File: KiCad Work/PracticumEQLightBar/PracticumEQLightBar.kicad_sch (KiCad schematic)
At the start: 54 parts, among them J1 AudioJack3Pin, U1 TEENSY 4.1, U2 TEENSY AUDIO ADAPTER BOARD RE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

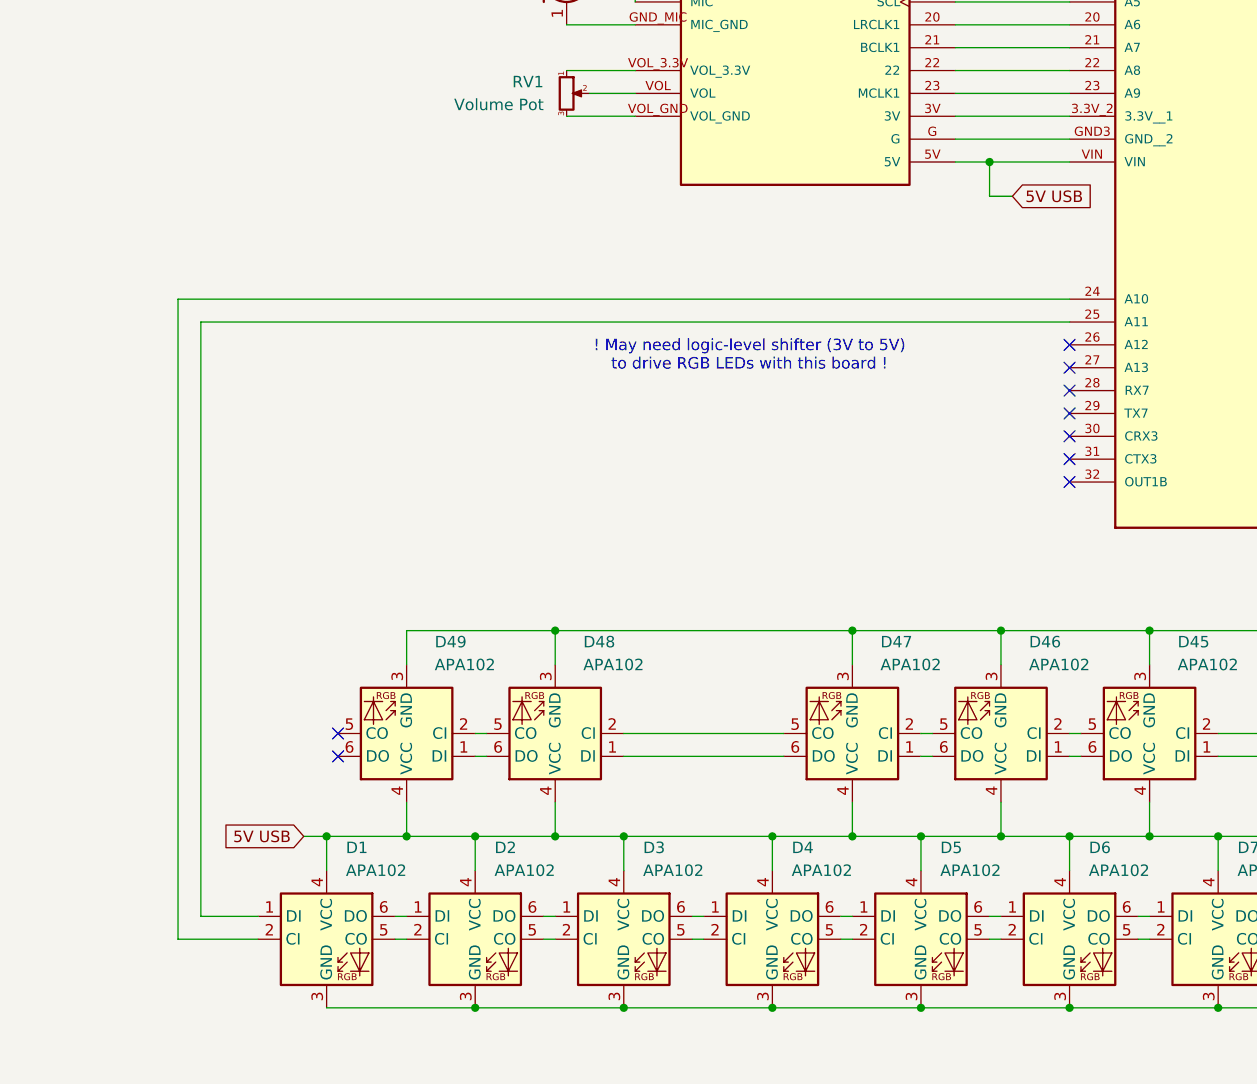
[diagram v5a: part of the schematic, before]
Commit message: Added SN74 logic level shifter to schematic and PCB
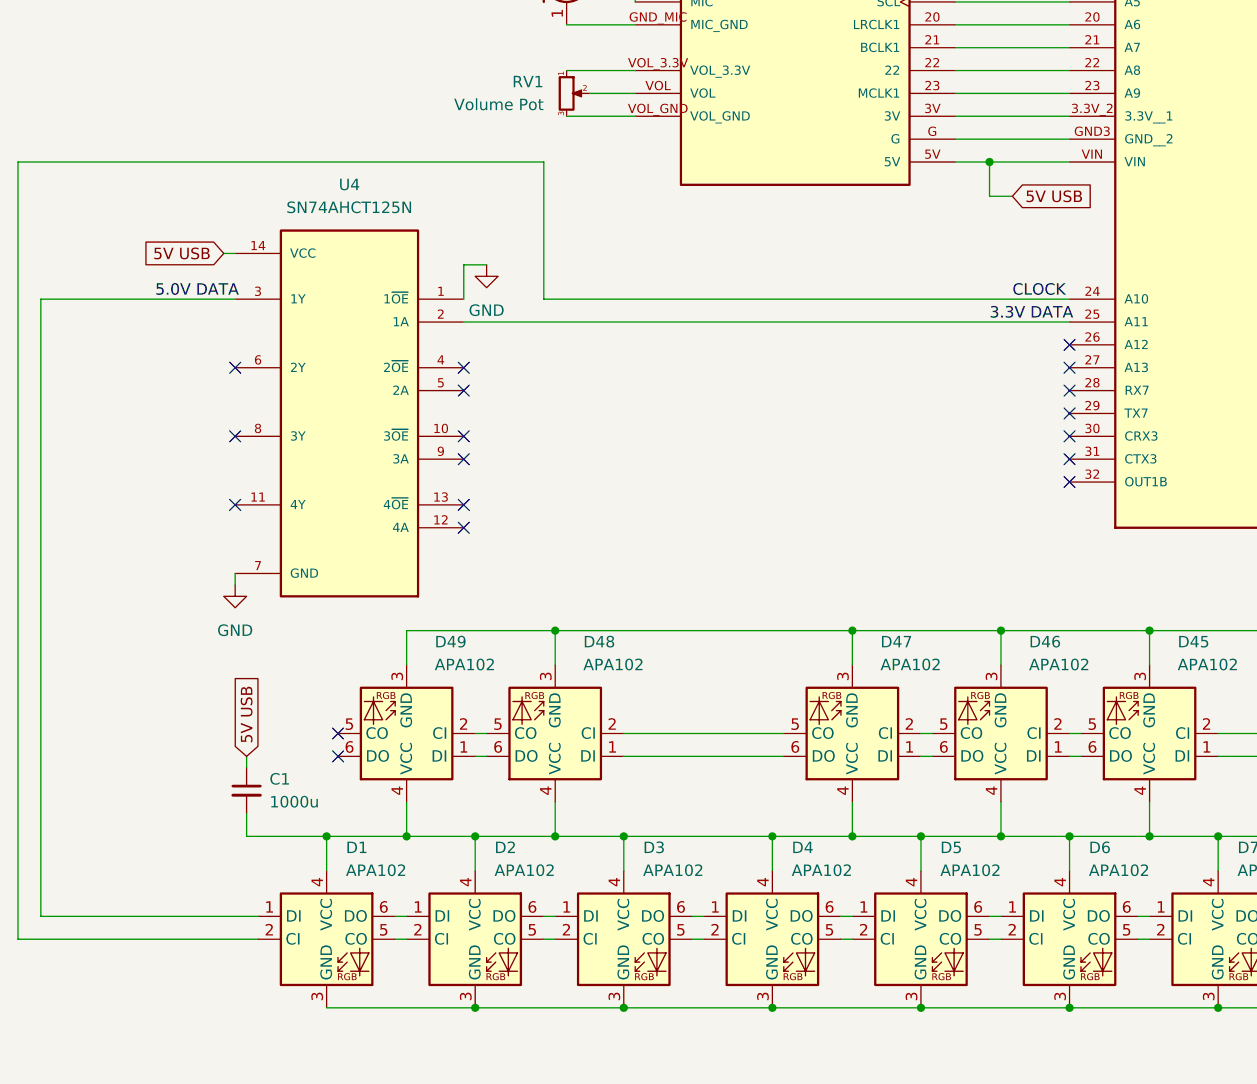
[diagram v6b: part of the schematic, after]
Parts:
- added C1: 1000u, symbol Device:C_Small
- added U4: SN74AHCT125N, SN74AHCT125N:DIP794W45P254L1930H508Q14, symbol SN74AHCT125N:SN74AHCT125N
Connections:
- net 5V USB: now also C1.1, U4.14 (VCC); no longer D1.4 (VCC), D10.4 (VCC), D11.4 (VCC), D12.4 (VCC), D13.4 (VCC), D14.4 (VCC), D15.4 (VCC), D16.4 (VCC), D17.4 (VCC), D18.4 (VCC), D19.4 (VCC), D2.4 (VCC), D20.4 (VCC), D21.4 (VCC), D22.4 (VCC), D23.4 (VCC), D24.4 (VCC), D25.4 (VCC), D26.4 (VCC), D27.4 (VCC), D28.4 (VCC), D29.4 (VCC), D3.4 (VCC), D30.4 (VCC), D31.4 (VCC), D32.4 (VCC), D33.4 (VCC), D34.4 (VCC), D35.4 (VCC), D36.4 (VCC), D37.4 (VCC), D38.4 (VCC), D39.4 (VCC), D4.4 (VCC), D40.4 (VCC), D41.4 (VCC), D42.4 (VCC), D43.4 (VCC), D44.4 (VCC), D45.4 (VCC), D46.4 (VCC), D47.4 (VCC), D48.4 (VCC), D49.4 (VCC), D5.4 (VCC), D6.4 (VCC), D7.4 (VCC), D8.4 (VCC), D9.4 (VCC)
- net GND: now also U4.1 (1~{OE}), U4.7 (GND)
- net CLOCK: now reaches D1.2 (CI), U1.24 (A10)
- net 3.3V DATA: now reaches U1.25 (A11)
- net 3.3V DATA: now also U4.2 (1A); no longer D1.1 (DI)
- new net: C1.2, D1.4 (VCC), D10.4 (VCC), D11.4 (VCC), D12.4 (VCC), D13.4 (VCC), D14.4 (VCC), D15.4 (VCC), D16.4 (VCC), D17.4 (VCC), D18.4 (VCC), D19.4 (VCC), D2.4 (VCC), D20.4 (VCC), D21.4 (VCC), D22.4 (VCC), D23.4 (VCC), D24.4 (VCC), D25.4 (VCC), D26.4 (VCC), D27.4 (VCC), D28.4 (VCC), D29.4 (VCC), D3.4 (VCC), D30.4 (VCC), D31.4 (VCC), D32.4 (VCC), D33.4 (VCC), D34.4 (VCC), D35.4 (VCC), D36.4 (VCC), D37.4 (VCC), D38.4 (VCC), D39.4 (VCC), D4.4 (VCC), D40.4 (VCC), D41.4 (VCC), D42.4 (VCC), D43.4 (VCC), D44.4 (VCC), D45.4 (VCC), D46.4 (VCC), D47.4 (VCC), D48.4 (VCC), D49.4 (VCC), D5.4 (VCC), D6.4 (VCC), D7.4 (VCC), D8.4 (VCC), D9.4 (VCC)
- new net 5.0V DATA: D1.1 (DI), U4.3 (1Y)
- no-connect marks 40 -> 49
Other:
- note removed: "! May need logic-level shifter (3V to 5V) to drive RGB LEDs with this board !"

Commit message: Updated rev 1.1 drawing sheet PDFs
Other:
- moved on the sheet: C1, D1, D10, D11, D12, D13, D14, D15, D16, D17, D18, D19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

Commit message: Commited wrong version last time
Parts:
- removed C1: 1000u, symbol Device:C_Small
- added TP1, TP2: TestPoint_Alt, TestPoint:TestPoint_Pad_1.5x1.5mm, symbol Connector:TestPoint_Alt
- U1: footprint EQLightBarLibrary:MODULE_DEV-16771 -> EQLightBarLibrary:Double PinSocket_1x24_P2.54mm_Vertical (Teensy 4_1)
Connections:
- net 3.3V DATA: now also U4.5 (2A), TP2.1; no longer U4.2 (1A)
- net 5V USB: now also D1.4 (VCC), D10.4 (VCC), D11.4 (VCC), D12.4 (VCC), D13.4 (VCC), D14.4 (VCC), D15.4 (VCC), D16.4 (VCC), D17.4 (VCC), D18.4 (VCC), D19.4 (VCC), D2.4 (VCC), D20.4 (VCC), D21.4 (VCC), D22.4 (VCC), D23.4 (VCC), D24.4 (VCC), D25.4 (VCC), D26.4 (VCC), D27.4 (VCC), D28.4 (VCC), D29.4 (VCC), D3.4 (VCC), D30.4 (VCC), D31.4 (VCC), D32.4 (VCC), D33.4 (VCC), D34.4 (VCC), D35.4 (VCC), D36.4 (VCC), D37.4 (VCC), D38.4 (VCC), D39.4 (VCC), D4.4 (VCC), D40.4 (VCC), D41.4 (VCC), D42.4 (VCC), D43.4 (VCC), D44.4 (VCC), D45.4 (VCC), D46.4 (VCC), D47.4 (VCC), D48.4 (VCC), D49.4 (VCC), D5.4 (VCC), D6.4 (VCC), D7.4 (VCC), D8.4 (VCC), D9.4 (VCC)
- net CLOCK: now also U4.2 (1A), TP1.1; no longer D1.2 (CI)
- net GND: now also U4.4 (2~{OE})
- net at U4.6 (2Y): now also D1.1 (DI)
- net 5.0V DATA: no longer names the net of U4.3 (1Y)
- net 5.0V DATA: now also D1.2 (CI); no longer D1.1 (DI)
- no-connect marks 49 -> 46
